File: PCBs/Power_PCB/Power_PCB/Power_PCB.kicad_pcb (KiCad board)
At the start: 4 copper layers, 90 x 175 mm, 96 parts, among them IC1 ADS1115BQDGSRQ1, IC10 ACS712ELCTR-20A-T, IC2 ADS1115BQDGSRQ1, IC3 W25Q16JVUXIQ_TR, IC7 ACS712ELCTR-20A-T, IC8 ACS712ELCTR-20A-T, IC9 ACS712ELCTR-20A-T, J1 Conn_01x02, J10 Conn_01x04, J11 Conn_01x04, J12 Conn_01x02, J13 Conn_01x04, J14 Conn_01x04, J15 8PCV-02-006, J16 8PCV-02-006, J17 8PCV-02-006, J18 8PCV-02-006, J2 Conn_01x02, J3 Conn_01x02, J4 Conn_01x02, J5 Conn_01x02, J6 Conn_01x02, J7 USB_C_Receptacle_USB2.0_16P, J8 Conn_01x02, J9 8PCV-02-006, Q1 SUD45P03-09, Q2 RQ6E080AJ, Q3 RQ6E080AJ, SW2 SW_Push, SW3 SW_Push, U1 ESP32-S3, U2 AMS1117-3.3, U3 USBLC6-2SC6, U5 TVS3300DRV, Y1 Crystal_GND24

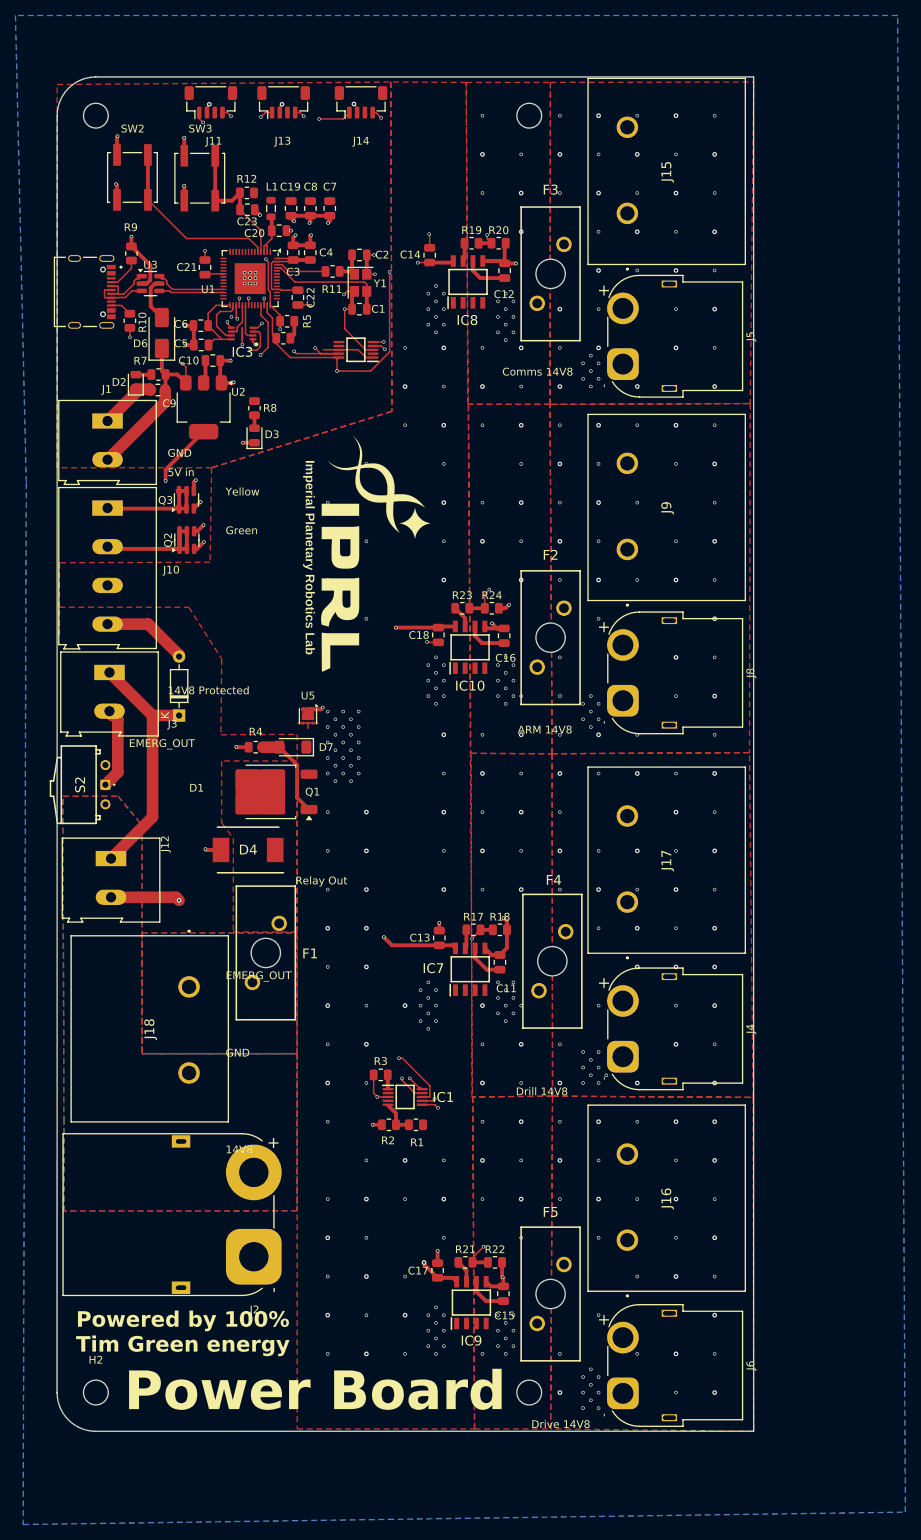
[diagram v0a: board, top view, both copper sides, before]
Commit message: Replaced fuse holders with 01000064Z
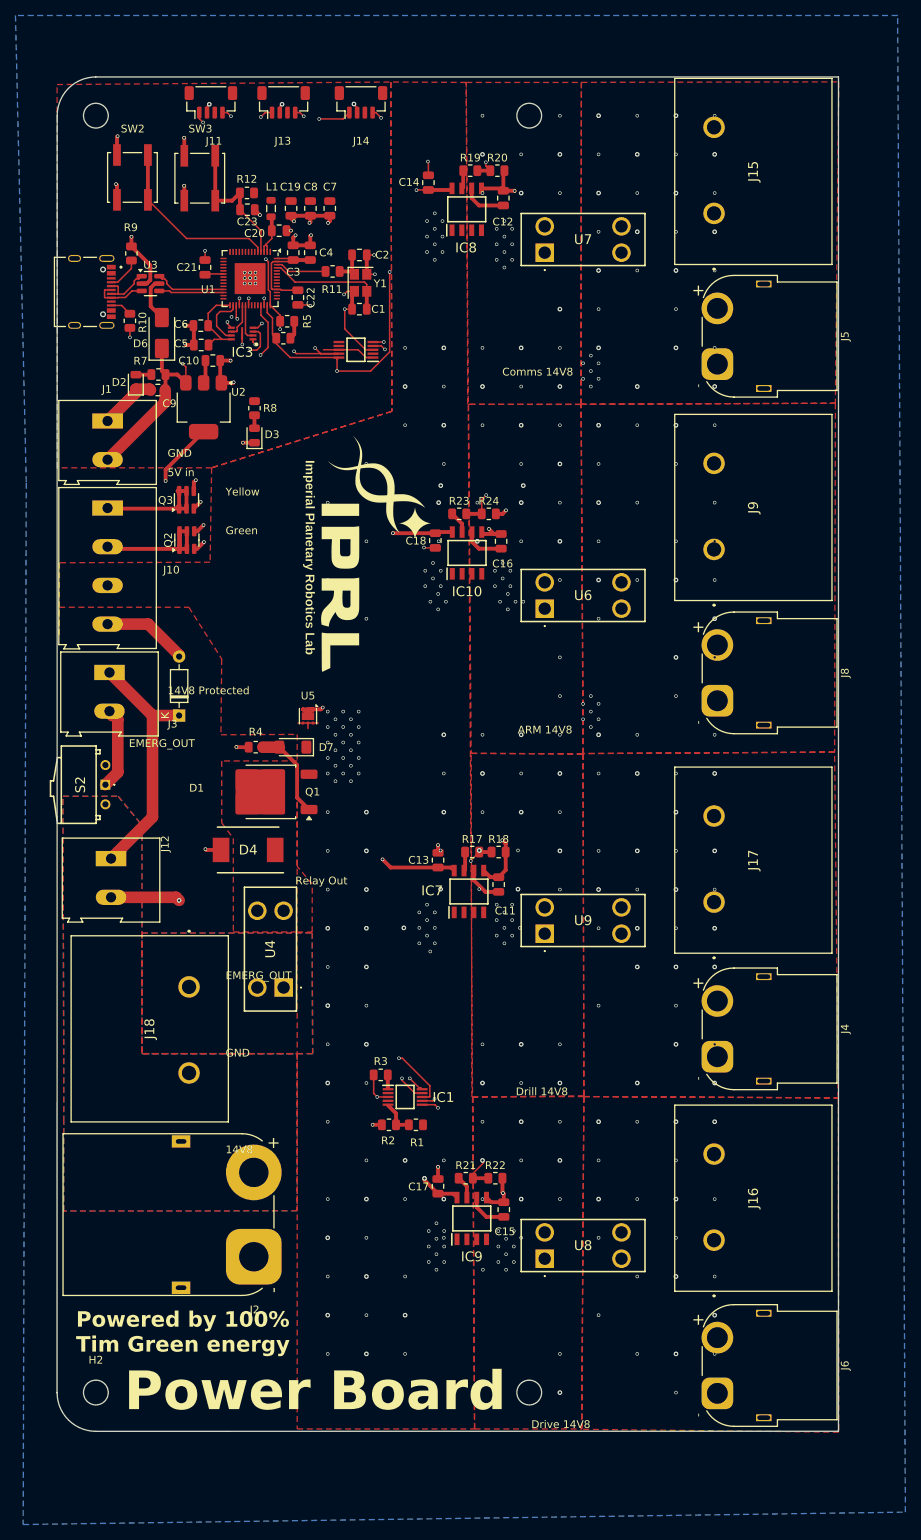
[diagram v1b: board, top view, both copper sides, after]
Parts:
- removed F1, F2, F3, F4, F5: 01530008Z, iprl_footprints:01530008
- added U4: 01000064Z, iprl_footprints:01000064Z, F.Cu at (82.5, 133.5)
- added U6: 01000064Z, iprl_footprints:01000064Z, F.Cu at (116.2, 84.5)
- added U7: 01000064Z, iprl_footprints:01000064Z, F.Cu at (116.2, 38.5)
- added U8: 01000064Z, iprl_footprints:01000064Z, F.Cu at (116.2, 168.5)
- added U9: 01000064Z, iprl_footprints:01000064Z, F.Cu at (116.2, 126.5)
- moved C16 12.2 mm to (110.6, 75.8)
- moved C18 12.2 mm to (102.1, 75.7)
- moved IC10 12.2 mm to (106.2, 77.3)
- moved R23 12.2 mm to (105.2, 72.2)
- moved R24 12.2 mm to (109.0, 72.2)
- moved J4 12.2 mm to (138.6, 142.4)
- moved J5 12.2 mm to (138.6, 52.9)
- moved J6 12.2 mm to (138.6, 185.9)
- moved J8 12.2 mm to (138.6, 96.4)
- moved J15 11.2 mm to (138.1, 33.4)
- moved J16 11.2 mm to (138.1, 166.1)
- moved J17 11.2 mm to (138.1, 122.4)
- moved J9 11.2 mm to (138.1, 76.8)
- moved C15 10.9 mm to (111.0, 162.2)
- moved C17 10.9 mm to (102.5, 159.2)
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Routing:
- net GND: vias 164 -> 162
- net /Current_sensing/COMMS_READ: vias 2 -> 1
- net /Connectors/14V8_DRILL_OUT: vias 24 -> 15
- net /Connectors/14V8_COMMS_OUT: vias 26 -> 17
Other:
- board size 90 x 175 mm -> 101 x 175 mm

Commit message: DRC clean after fuse holder replacement
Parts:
- moved H3 14.0 mm to (128.2, 185.8)
- moved H1 14.0 mm to (128.2, 20.8)
- moved IC8 0.17 mm to (106.0, 32.9)
- moved R19 0.17 mm to (106.5, 27.9)
- moved R20 0.17 mm to (110.0, 27.9)
- moved C12 0.16 mm to (110.7, 31.4)
- moved C14 0.16 mm to (101.0, 29.4)
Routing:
- net /Current_sensing/ARM_READ: track 43.0 -> 30.2 mm
- net /Current_sensing/COMMS_READ: track 27.2 -> 15.2 mm, vias 1 -> 2
- net /Current_sensing/DRILL_READ: track 28.1 -> 37.6 mm
- net /Current_sensing/DRIVE_READ: track 24.2 -> 31.5 mm
- net +5V: track 300.3 -> 304.1 mm
- net /SDA: track 175.3 -> 173.8 mm
- net GND: vias 162 -> 248
- net /Connectors/14V8_DRIVE_OUT: vias 23 -> 35
- net /Connectors/14V8_DRILL_OUT: vias 15 -> 38
- net /Connectors/14V8_COMMS_OUT: vias 17 -> 38
- net /Connectors/14V8_ARM_OUT: vias 28 -> 38
- net /14V8_PROTECTED: vias 98 -> 119
- net /14V8_DRIVE_OUT: vias 15 -> 20
- net /14V8_DRILL_OUT: vias 16 -> 20
- net /14V8_COMMS_OUT: vias 14 -> 19
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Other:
- board text added: "14V_IN"
- board text added: "5V"
- board text removed: "14V8"

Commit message: submitted power board
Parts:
- removed Q1: SUD45P03-09, Package_TO_SOT_SMD:TO-252-2
- removed S2: EGJ1210AAT2, iprl_footprints:EGJ1210AAT2
- added Q4: NTD25P03LT4G, iprl_footprints:MJD45H11T4G, F.Cu at (82.6, 108.0)
- added S1: SK12F14G5, iprl_footprints:SK12F14G5, F.Cu at (57.2, 106.8)
- D1: value 1N4148 -> 1N4148WT; footprint Diode_THT:D_DO-35_SOD27_P7.62mm_Horizontal -> iprl_footprints:SODFL1608X70N
- J11, J13, J14: footprint Connector_JST:JST_SH_BM04B-SRSS-TB_1x04-1MP_P1.00mm_Vertical -> Connector_JST:JST_PH_S4B-PH-K_1x04_P2.00mm_Horizontal
- J15, J16, J17, J18, J9: value 8PCV-02-006 -> YK4420203000G; footprint iprl_footprints:8PCV02006 -> iprl_footprints:RHDR2W120P0X950_1X2_2050X1430X1790P
- U2: value AMS1117-3.3 -> 178.6164.0001; footprint Package_TO_SOT_SMD:SOT-223-3_TabPin2 -> iprl_footprints:178.6164.XXX1
- U4, U6, U7, U8: value 01000064Z -> 178.6164.0001; footprint iprl_footprints:01000064Z -> iprl_footprints:178.6164.XXX1
- U9: value 01000064Z -> AMS1117-3.3; footprint iprl_footprints:01000064Z -> Package_TO_SOT_SMD:SOT-223-3_TabPin2
- moved U9 80.9 mm to (72.2, 58.6), turned to -90 degrees
- moved U2 55.3 mm to (121.2, 84.0), turned to 0 degrees
- moved J16 54.8 mm to (145.4, 111.8), turned to -90 degrees
- moved J9 53.7 mm to (146.2, 23.8), turned to -90 degrees
- moved U6 41.6 mm to (121.2, 125.8)
- moved J17 34.5 mm to (145.9, 156.1), turned to -90 degrees
- moved J15 33.6 mm to (145.9, 66.0), turned to -90 degrees
- moved J18 12.3 mm to (68.5, 145.6), turned to 90 degrees
- moved U8 5.38 mm to (121.6, 168.0)
- moved J12 5.00 mm to (60.2, 121.8)
- moved U7 4.42 mm to (120.6, 37.8)
- moved D1 4.01 mm to (69.0, 94.3)
- moved J14 3.82 mm to (94.9, 22.1), turned to 180 degrees
- moved J13 3.29 mm to (83.8, 22.1), turned to 180 degrees
- moved J11 3.05 mm to (72.7, 22.1), turned to 180 degrees
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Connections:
- J15 pad 2: /Connectors/14V8_DRIVE_OUT -> /Connectors/14V8_ARM_OUT
- J16 pad 2: /Connectors/14V8_COMMS_OUT -> /Connectors/14V8_DRILL_OUT
- J17 pad 2: /Connectors/14V8_DRILL_OUT -> /Connectors/14V8_COMMS_OUT
- J18 pad 1: /Power/RELAY_OUT -> /Power/14V8_IN
- J18 pad 2: /Power/14V8_IN -> /Power/RELAY_OUT
- J9 pad 2: /Connectors/14V8_ARM_OUT -> /Connectors/14V8_DRIVE_OUT
- U2 pad 1: GND -> /14V8_ARM_OUT
- U2 pad 2: +3.3V -> /Connectors/14V8_ARM_OUT
- U6 pad 1: /14V8_ARM_OUT -> /14V8_DRILL_OUT
- U6 pad 2: /Connectors/14V8_ARM_OUT -> /Connectors/14V8_DRILL_OUT
- U9 pad 1: /14V8_DRILL_OUT -> GND
- U9 pad 2: /Connectors/14V8_DRILL_OUT -> +3.3V
- U9 pad 3: /Connectors/14V8_DRILL_OUT -> +5V
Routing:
- net /Power/EMERG_OUT: track 32.0 -> 38.4 mm
- net Net-(J3-Pin_2): track 11.1 -> 16.5 mm
- net /SDA: track 173.8 -> 178.5 mm
- net /SCL: track 178.9 -> 181.6 mm
- net GND: track 149.4 -> 151.2 mm, vias 248 -> 251
- net +5V: track 304.1 -> 303.0 mm
- net /Connectors/14V8_DRIVE_OUT: vias 35 -> 36
- net /Connectors/14V8_DRILL_OUT: vias 38 -> 39
- net /14V8_PROTECTED: vias 119 -> 117
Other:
- board text added: "The unorthodox is always worth trying"
